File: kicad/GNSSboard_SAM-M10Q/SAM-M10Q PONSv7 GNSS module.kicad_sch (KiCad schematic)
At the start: 8 parts, among them J1 2005280040, U2 SAM-M10Q-00B

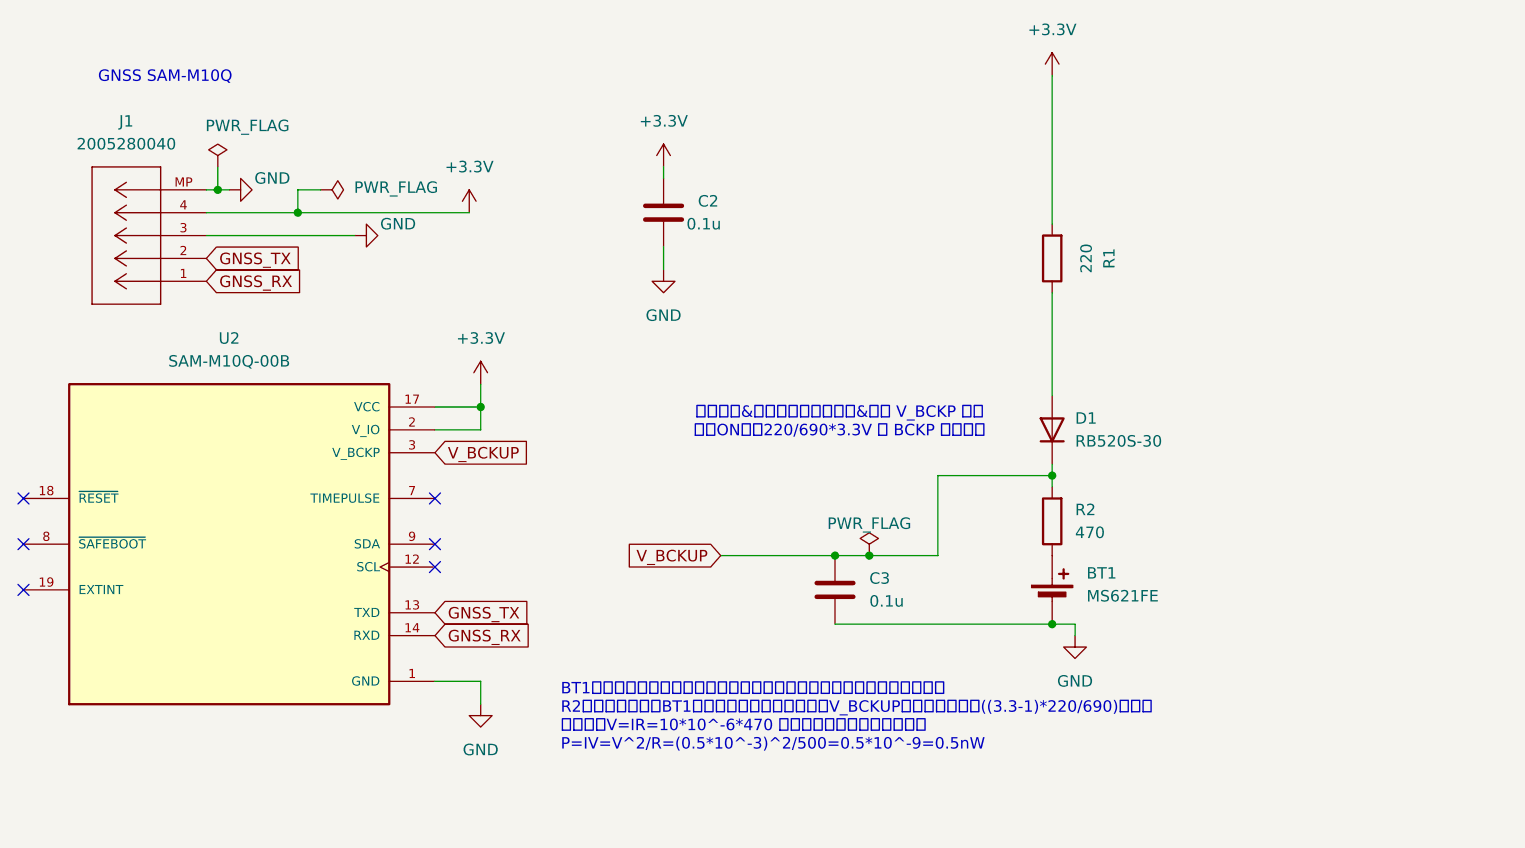
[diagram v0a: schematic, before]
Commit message: 0.986 新基板（SCH16T 外付け）の kicad を追加し、ガーバー出力を git から外した
kicad/IMU_murata/ — SCH16T-K01-10 のブレイクアウト（新規）
本体の J7（Molex 200528-0080・8pin FPC）へ 1:1 ケーブルで繋ぐ外付け基板。
J1 のピン順を本体 J7 と一致させてある（1=+3V3 2=RESET 3=MOSI 4=CS 5=SCK
6=SYNC 7=MISO 8=GND）。シンボルとフットプリントも同梱。
- ★ R2（CS-GND の 4.7k）は実装しない。CS は負論理なので、プルダウンすると
  MCU が駆動していない間セレクト状態になる。R1（EXTRESN プルアップ）は実装する
- 本体側の GPIO 割り当ては settings.h の SCH16T_PIN_* が正本
  （一覧は docs/imu_sch16t_plan.md §3）

mainboard / GNSS モジュールの更新
- mainboard: DisplayModule_PONSv7 の pcb / pro / sch、MS5611BNO085.kicad_sch、
  SHT_RP2354B.kicad_sch
- GNSS モジュール: pcb / pro / sch、および QRv7 と FPC 4p のフットプリントを
  同プロジェクトの Footprints/ へ取り込み

kicad/FPC/ を畳んだ
FPC コネクタ 1 個のためのプロジェクトだったので、フットプリントを
kicad/GNSSboard_SAM-M10Q/Footprints/ へ移して削除した。
中身は同じで、差分は KiCad が再生成する uuid だけ。

ガーバー・ドリルのプロット出力を git から外した
kicad/.gitignore に追加（*.gbr *.gbl *.gbs *.gbp *.gbo *.gm1 *.gtl *.gts
*.gtp *.gto *.drl と、保険の *plot/ *plot.zip）。発注のたびに作り直せるうえ、
基板を直すたびに巨大な差分になる（ルート .gitignore の production/ と同じ理由）。
★ 入れ物のフォルダ名で書かないこと。v5_1plot/ のような名前は付け方が毎回違うので
  次の基板で外れる。既存の *-backups/ / *.kicad_prl と同じ方針。

Co-Authored-By: Claude Opus 5 <noreply@anthropic.com>
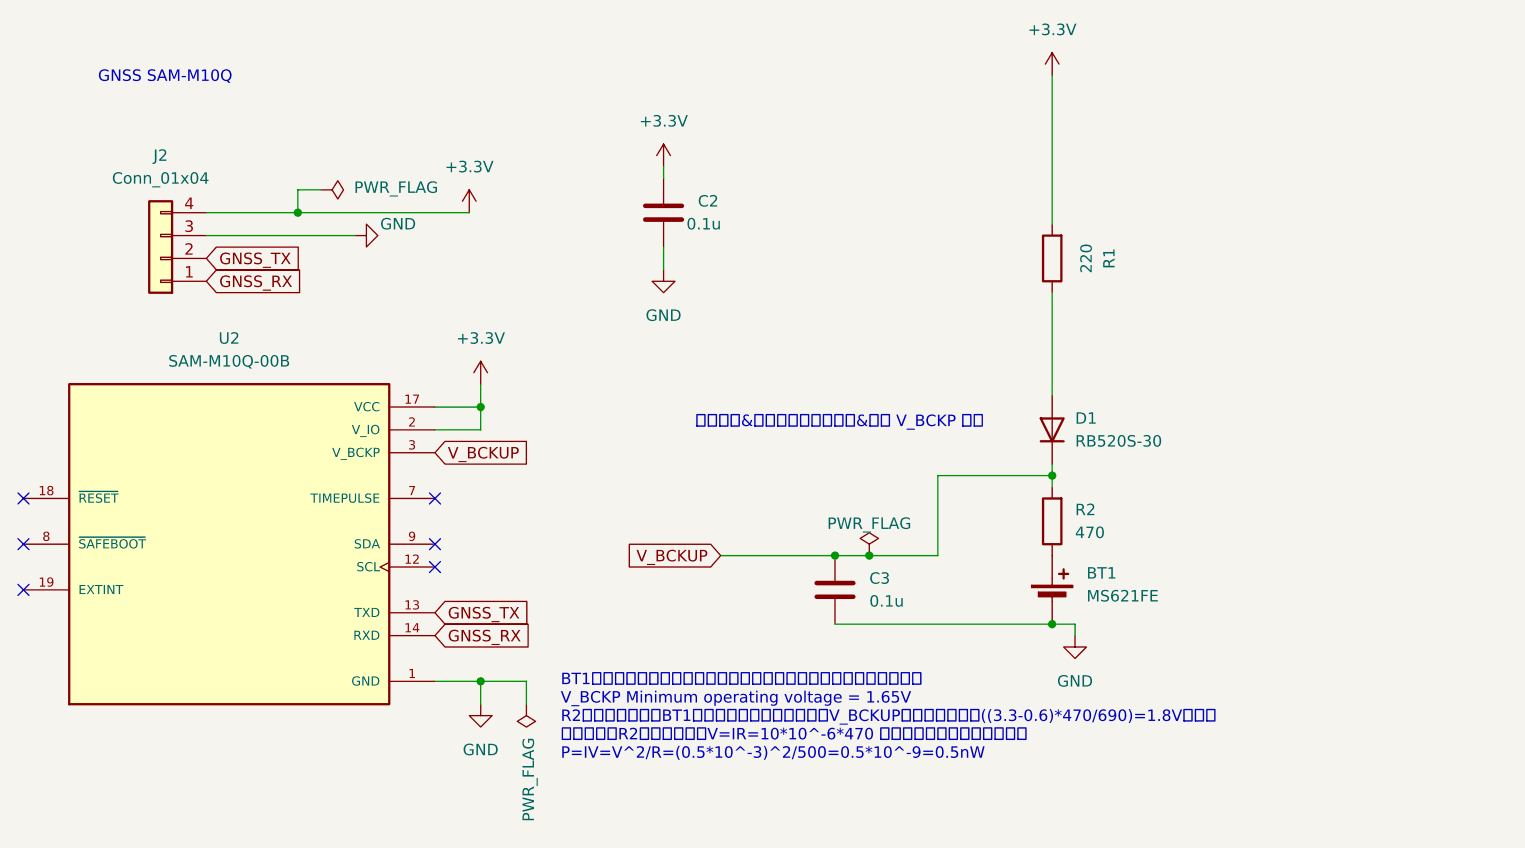
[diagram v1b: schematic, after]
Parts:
- removed J1: 2005280040, Connector_FFC-FPC:Molex_200528-0040_1x04-1MP_P1.00mm_Horizontal, symbol 2005280040:2005280040
- added J2: Conn_01x04, GPS_TFT:FPC_CON 4p 1mm, symbol Connector_Generic:Conn_01x04
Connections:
- net +3.3V: now also J2.4 (Pin_4)
- net GND: now also J2.3 (Pin_3)
- net GNSS_RX: now also J2.1 (Pin_1)
- net GNSS_TX: now also J2.2 (Pin_2)
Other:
- note added: "BT1が放電しきっていると、モジュールが起動しないバグがあった。 V_BCKP Minimum operating voltage = 1.65V R2抵抗によって、BT1バッテリーが空っぽでも、V_BCKUPに電圧が生じる((3.3-0.6)*470/690)=1.8Vぐらい 放電時は、R2の電圧降下はV=IR=10*10^-6*470 で、電圧降下はほとんどない P=IV=V^2/R=(0.5*10^-3)^2/500=0.5*10^-9=0.5nW"
- note added: "突入電流&バッテリー電流制限&最小 V_BCKP 対策"
- note removed: "BT1が放電しきっていると、モジュールが起動しないバグがあったため、 R2抵抗によって、BT1バッテリーが空っぽでも、V_BCKUPに電圧が生じる((3.3-1)*220/690)ぐらい 放電は、V=IR=10*10^-6*470 で、電圧降下はほとんどない P=IV=V^2/R=(0.5*10^-3)^2/500=0.5*10^-9=0.5nW"
- note removed: "突入電流&バッテリー電流制限&最小 V_BCKP 対策 電源ONで、220/690*3.3V が BCKP にかかる"

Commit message: 0.993 v7.1 基板の回路図と PCB を仕上げ、SW OFF のままの充電と電源異常を画面と音声で知らせるようにした
- power.cpp（新規）: USB の判定を usb_power_present() に一本化（v7.1 は VBUS を
  GPIO47 の ADC で測る）。電源経路の異常（2026-10-15 の充電 IC 焼損）を検出し、
  地図の POWER FAULT!! と power_fault.wav（30 秒ごと・最低音量 60）で知らせる。
  受信機は LINK_ST_PWR_FAULT を受けてトーン（同じ音声だとボートへの指示に聞こえる）
- v7.1: SW を OFF にしたまま USB で充電していると満充電にならない（Q3 のボディ
  ダイオード経由）。SW4 の OFF 側が GPIO40 を GND に落とすのを読み、地図に注意を出し
  1 度だけ読み上げる（charge_sw_off / charge_sw_on。排他グループ WAV_EXCL_CHARGE_SW）。
  移動中・ミラー中・リプレイ中・デモ中は出さない。判定に USB を入れない
  （VBUS が一瞬 4.3V を割ると 0V が本物の電池電圧として流れるため）。このあいだは
  電池低下の警告を止め、無線は RHAVE_VOLT を立てず LINK_ST_USB_SW_OFF、CSV は空欄
- 受信モードの電池表示を s55r42 の形に。SW OFF のまま USB の側は s5V / r5V
- backlight.cpp（新規）: v7.1 のバックライト PWM と VEML7700 の自動調光。
  飛行 CSV に lux / backlight 列
- E220 の M0/M1 は v7.1 で GPIO31 へ（GPIO47 は USB_SENS）
- 本体の回路図・PCB: SCH16T の J6 を逆順に（完成済みの FPC で J6-n ↔ J3-(9-n)）、
  F1 0805L035 → 0805L050（夏の充電で切れない）、R34/R35 を 10k/5.1k、C32 を 10µF 0805、
  SPI1 の SCK/MOSI/CS に 33Ω（R49〜R51）、スライドスイッチを MST-12D18G2 に、
  回路図とつながらない旧フットプリント（C33/R37/R38/R11 470Ω）を削除、DNP の BOM 除外、
  CUS-12TB の残骸とライブラリ登録を削除、メモの部品番号を v7.1 に
- GNSS 基板を 5 ピン（V_BCKUP）に。バックアップ電池は本体へ移した
- case_cover（照度センサー VEML7700）の kicad を追加。IMU ブレイクアウトの R2 を DNP
- 音声 3 本（power_fault / charge_sw_off / charge_sw_on）は macOS の音声合成の仮音声
- docs/pons_power.md（新規）。README の「自作の手順」を v7.1 に書き直し、
  SCH16T の配線の記述（J7・1:1 ケーブル）を J6・逆順に直した
- gen_wav_flash.py はコメント中の引用符付きの音声名も拾うので、録音前の名前を書かない

PONS_BOARD は V7 と V71 の両方でビルド OK（3,929,776 / 3,923,504 B）/
gen_wav_flash.py --check は 35 ファイル一致 / 本体 PCB の DRC は未配線 0・回路図と一致
（シルクの 6 件はボタンと USB の突起で意図どおり）/ GNSS 基板も未配線 0 / 実機は未確認

Co-Authored-By: Claude Opus 5.5 <noreply@anthropic.com>
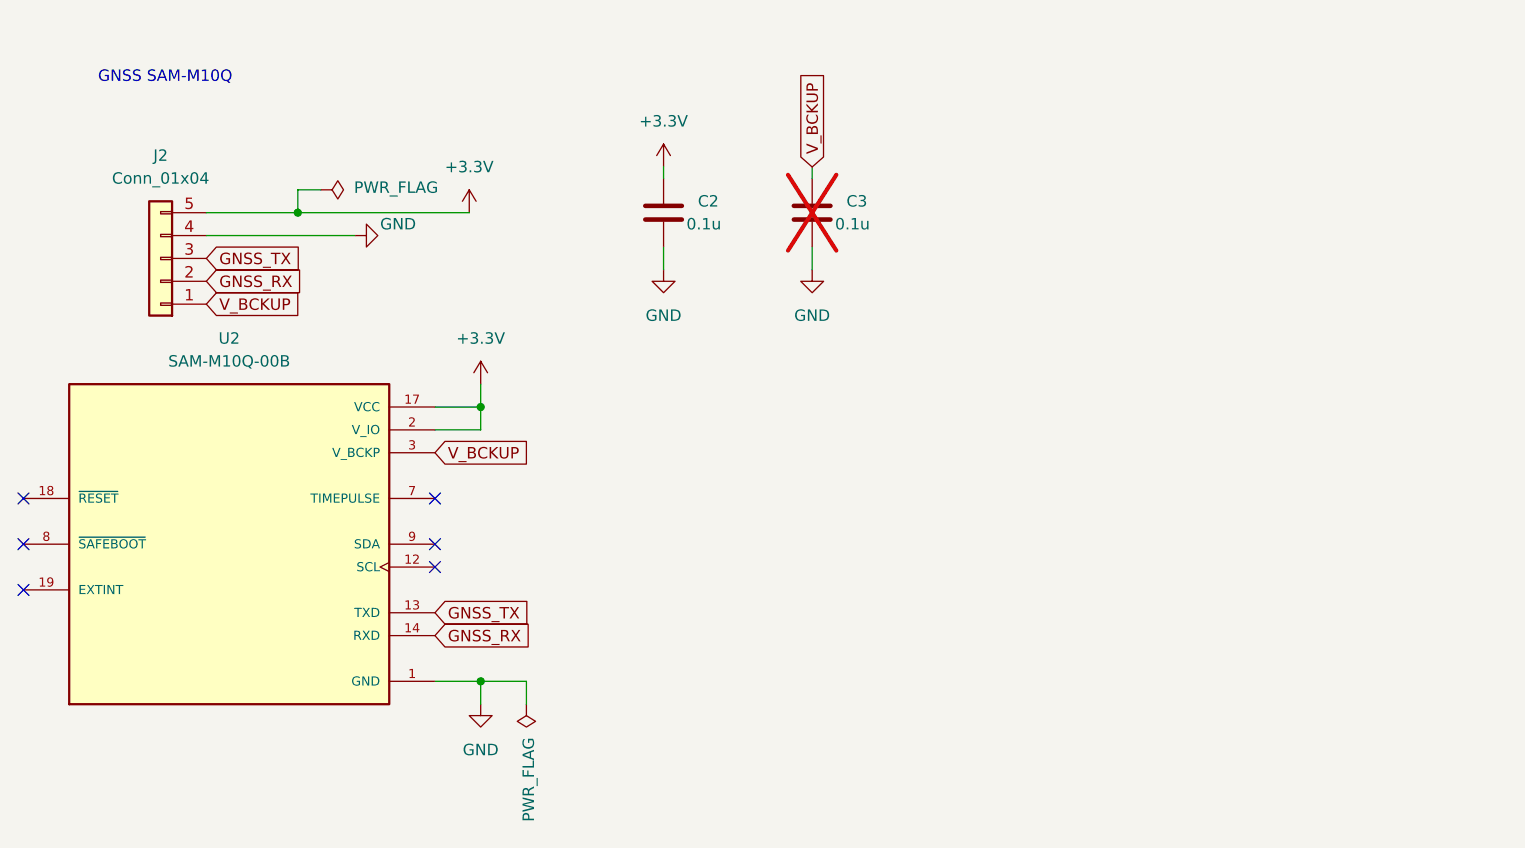
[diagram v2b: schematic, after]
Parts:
- removed BT1: MS621FE, Battery:BatteryHolder_Seiko_MS621F, symbol Device:Battery_Cell
- removed D1: RB520S-30, Diode_SMD:D_SOD-523, symbol Diode:1N4001
- removed R1: 220, Resistor_SMD:R_0603_1608Metric_Pad0.98x0.95mm_HandSolder, symbol Device:R
- removed R2: 470, Resistor_SMD:R_0603_1608Metric_Pad0.98x0.95mm_HandSolder, symbol Device:R
- C3: now not fitted
- J2: footprint GPS_TFT:FPC_CON 4p 1mm -> GPS_TFT:FPC_CON 5p 1mm; symbol Connector_Generic:Conn_01x04 -> Connector_Generic:Conn_01x05
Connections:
- net +3.3V: now also J2.5 (Pin_5); no longer J2.4 (Pin_4)
- net GND: now also J2.4 (Pin_4); no longer J2.3 (Pin_3)
- net GNSS_RX: now also J2.2 (Pin_2); no longer J2.1 (Pin_1)
- net GNSS_TX: now also J2.3 (Pin_3); no longer J2.2 (Pin_2)
- net V_BCKUP: now also J2.1 (Pin_1)
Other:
- note removed: "BT1が放電しきっていると、モジュールが起動しないバグがあった。 V_BCKP Minimum operating voltage = 1.65V R2抵抗によって、BT1バッテリーが空っぽでも、V_BCKUPに電圧が生じる((3.3-0.6)*470/690)=1.8Vぐらい 放電時は、R2の電圧降下はV=IR=10*10^-6*470 で、電圧降下はほとんどない P=IV=V^2/R=(0.5*10^-3)^2/500=0.5*10^-9=0.5nW"
- note removed: "突入電流&バッテリー電流制限&最小 V_BCKP 対策"

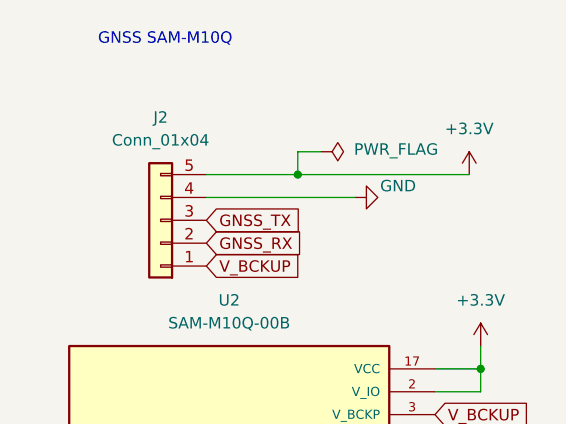
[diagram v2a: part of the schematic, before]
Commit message: 0.994 GNSS の翌日起動を速くし、本番前チェック・高温充電の警告・電池低下の点滅を入れ、v7.1 基板の逆接保護と発注前の修正を仕上げた
- GNSS: AssistNow Autonomous を有効化（CFG-VALSET で RAM と BBR。settings.h の
  GNSS_USE_ANA。0 でも OFF を書き込む＝BBR に残った ON を消すため）。前日と同じ時間帯の
  起動が 23〜28 秒 → 3〜4 秒（BT1 が生きていること）。NAV-AOPSTATUS を 1Hz で受け、
  GNSS DETAIL 3 に ANA:ON data/use/calc、log.txt に「... after boot」（TTFF）・最初の
  測位の軌道の出どころ・10 分ごとの計算時間。ACK 待ちの間も imu_service_if_due() を
  呼ぶ（以前からの抜け）
- readiness.cpp（新規）: 本番前チェック。GNSS・IMU・ESKF・較正（マウント外れだけ。
  日付またぎは推測なので入れない＝台の上での APPLY を促さない）・地上の姿勢・設定画面の
  赤丸・USB・電池 50%・SD・無線（送信モード）がそろい、地上で止まっていたら 1 度だけ
  「準備完了」（ready.wav）。欠けていれば設定画面の右上に項目名。受信モード・リプレイ・
  デモは対象外。既存の判定を読むだけで、条件は書き写さない
- 高温での充電の警告（v7・v7.1）: USB 接続中に MS5611 が 45°C を 30 秒超え続けたら
  地図に TOO HOT TO CHARGE と charge_hot.wav（60 秒ごと・最低音量 60）。電池の仕様は
  充電 0〜45°C。地図の段は電源異常と共用（異常 ＞ 高温 ＞ SW OFF）
- 電池低下のときの点滅（v7.1）: 電池低下の警告と同じ 3.5V でバックライトを 2 秒点灯・
  4 秒消灯。3.65V か USB で戻る（3.5V で戻すと入り切りをくり返す）。消灯中も本来の
  明るさは追い続ける（照度追従の立ち上がりで 2 秒の点灯が暗くならないように）
- 本体の回路図・PCB: 電池の逆接保護 Q4（AO3401A、D が電池側）＋ R52、PWR1 の
  ネットを VBAT_RAW に。C32 を 10µF 0805 に（10/20 に直したのが 0402 に戻っていた）。
  D5 を RB751S40（逆流が少ない。PCBA で実装）に。古いメモを整理
- IMU 基板の GND が IC1.16・C3 だけ分かれていたのをつないだ。J3 の値を 01x08 に。
  case_cover の部品番号を回路図と一致。GNSS 基板の裏面を GND ベタに（浮いていた
  19 個のビアがつながった）
- 音声 2 本（ready / charge_hot）は macOS の音声合成の仮音声
- docs: pons_power.md に Q4・P-ch FET 3 段の役割・電池の保護回路（DTP603048(PHR) の
  仕様書）・R39 を 2.2kΩ に戻さない理由（電池の最大充電 430mA も超える）・高温の警告・
  電池低下の点滅。README に GNSS の起動・本番前チェック・新しい警報・v7.1 の USB-C と
  充電時間、古い記述（v7 の実結線試験・無線の立ち上げ手順書の冒頭）を今の状態に。
  CLAUDE.md に BBR に書いた GNSS 設定が残る件と readiness.cpp
- kicad/.gitignore に *.pos

PONS_BOARD は V7 と V71 の両方でビルド OK（4,052,376 / 4,046,728 B）/
gen_wav_flash.py --check は 37 ファイル一致 / 本体 PCB の DRC は未配線 0・回路図と一致
（シルクの 6 件は意図どおり）/ IMU・カバー・GNSS 基板も未配線 0・回路図と一致 /
BOM の LCSC 番号は全 48 種類を JLC/LCSC の部品情報と照合 / 実機は未確認

Co-Authored-By: Claude Opus 5.5 <noreply@anthropic.com>
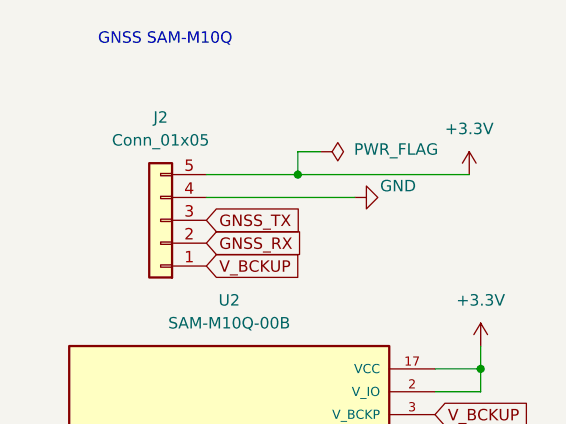
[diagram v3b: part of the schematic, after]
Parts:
- J2: value Conn_01x04 -> Conn_01x05
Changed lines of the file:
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@@
 			)
 		)
-		(property "Value" "Conn_01x04"
+		(property "Value" "Conn_01x05"
 			(at 69.85 59.69 0)
 			(show_name no)

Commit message: 0.995 無線で化けたフレームを数え直していたのを直し、仮の音声 5 つを録音に差し替え、画面のセンサー名を基板に合わせ、起動ロゴを生成ツールで焼くようにし、README を v7.1 の発注方法に書き直した
Co-Authored-By: Claude Opus 5.5 <noreply@anthropic.com>
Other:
- title: SAM-M10Q PONSv7 GNSS module -> SAM-M10Q PONS GNSS module
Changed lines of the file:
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@@
 	(paper "A4")
 	(title_block
-		(title "SAM-M10Q PONSv7 GNSS module")
-		(date "2026-09-06")
-		(rev "1.0")
+		(title "SAM-M10Q PONS GNSS module")
+		(date "2026-10-22")
+		(rev "7.1")
 	)
 	(text "GNSS SAM-M10Q"
